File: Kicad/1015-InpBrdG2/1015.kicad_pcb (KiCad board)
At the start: 2 copper layers, 44.5 x 20.3 mm, 10 parts, among them P1 TST, P2 CONN_4, P3 CONN_4, P4 CONN_6, P5 CONN_8, P6 CONN_4

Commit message: Updates to silkscreen and created mashup.  These Gerbers sent to PCB house.
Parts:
- R1: value 100K -> 0
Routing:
- added copper zone on B.Cu, net GND
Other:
- board text added: "CLK"
- board text added: "MISO"
- board text added: "MOSI"
- board text added: "SSEL"
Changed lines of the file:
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@@
     (links 18)
     (no_connects 0)
-    (area 221.843599 152.39619 267.97127 176.403)
+    (area 220.904999 154.533599 265.836401 175.831501)
     (thickness 1.6)
-    (drawings 4)
+    (drawings 8)
     (tracks 21)
     (zones 0)
@@
   )
   (setup
-    (last_trace_width 0.889)
-    (user_trace_width 0.889)
+    (last_trace_width 0.254)
+    (user_trace_width 1.27)
     (trace_clearance 0.254)
-    (zone_clearance 0.254)
+    (zone_clearance 0.508)
     (zone_45_only no)
     (trace_min 0.254)
@@
     (autoplace_cost90 10)
     (autoplace_cost180 10)
-    (fp_text reference R2 (at -1.016 2.54 180) (layer F.SilkS)
-      (effects (font (size 1.397 1.27) (thickness 0.2032)))
-    )
-    (fp_text value 480 (at -1.143 2.54 180) (layer F.SilkS) hide
+    (fp_text reference R2 (at 3.81 0 180) (layer F.SilkS)
+      (effects (font (size 1.397 1.27) (thickness 0.2032)))
+    )
+    (fp_text value 480 (at -0.635 -0.635 180) (layer F.SilkS) hide
       (effects (font (size 1.397 1.27) (thickness 0.2032)))
     )
@@
     (autoplace_cost90 10)
     (autoplace_cost180 10)
-    (fp_text reference R3 (at -1.016 2.54 180) (layer F.SilkS)
-      (effects (font (size 1.397 1.27) (thickness 0.2032)))
-    )
-    (fp_text value 480 (at -1.143 2.54 180) (layer F.SilkS) hide
+    (fp_text reference R3 (at 3.81 0 180) (layer F.SilkS)
+      (effects (font (size 1.397 1.27) (thickness 0.2032)))
+    )
+    (fp_text value 480 (at 0 0 180) (layer F.SilkS) hide
       (effects (font (size 1.397 1.27) (thickness 0.2032)))
     )
@@
     (autoplace_cost90 10)
     (autoplace_cost180 10)
-    (fp_text reference R4 (at -1.016 2.54 180) (layer F.SilkS)
-      (effects (font (size 1.397 1.27) (thickness 0.2032)))
-    )
-    (fp_text value 480 (at -1.143 2.54 180) (layer F.SilkS) hide
+    (fp_text reference R4 (at 3.81 -0.635 180) (layer F.SilkS)
+      (effects (font (size 1.397 1.27) (thickness 0.2032)))
+    )
+    (fp_text value 480 (at 0 0 180) (layer F.SilkS) hide
       (effects (font (size 1.397 1.27) (thickness 0.2032)))
     )
@@
   (module 00_th1x6x100-lock (layer F.Cu)
     (at 239.395 162.56 270)
-    (fp_text reference P4 (at -6.35 5.08 360) (layer F.SilkS)
+    (fp_text reference P4 (at 5.08 -5.08 270) (layer F.SilkS)
       (effects (font (size 1.524 1.524) (thickness 0.3048)))
     )
@@
       (effects (font (size 1.397 1.27) (thickness 0.2032)))
     )
-    (fp_text value 100K (at 0 0.127 180) (layer F.SilkS)
+    (fp_text value 0 (at 0 0.127 180) (layer F.SilkS)
       (effects (font (size 1.397 1.27) (thickness 0.2032)))
     )
@@
     )
   )
+  (gr_text SSEL (at 245.745 163.195) (layer F.SilkS)
+    (effects (font (size 1.5 1.5) (thickness 0.3)))
+  )
+  (gr_text CLK (at 245.11 161.29) (layer F.SilkS)
+    (effects (font (size 1.5 1.5) (thickness 0.3)))
+  )
+  (gr_text MISO (at 245.745 158.75) (layer F.SilkS)
+    (effects (font (size 1.5 1.5) (thickness 0.3)))
+  )
+  (gr_text MOSI (at 245.745 156.21) (layer F.SilkS)
+    (effects (font (size 1.5 1.5) (thickness 0.3)))
+  )
   (gr_line (start 265.43 154.94) (end 220.98 154.94) (angle 90) (layer Edge.Cuts) (width 0.15))
   (gr_line (start 265.43 175.26) (end 265.43 154.94) (angle 90) (layer Edge.Cuts) (width 0.15))
   (gr_line (start 220.98 175.26) (end 265.43 175.26) (angle 90) (layer Edge.Cuts) (width 0.15))
   (gr_line (start 220.98 154.94) (end 220.98 175.26) (angle 90) (layer Edge.Cuts) (width 0.15))
-  (segment (start 226.06 156.21) (end 226.06 173.99) (width 0.889) (layer F.Cu) (net 1) (status C00000))
-  (segment (start 228.6 156.21) (end 228.6 173.99) (width 0.889) (layer F.Cu) (net 2) (status C00000))
+  (segment (start 226.06 156.21) (end 226.06 173.99) (width 1.27) (layer F.Cu) (net 1))
+  (segment (start 228.6 156.21) (end 228.6 173.99) (width 1.27) (layer F.Cu) (net 2))
   (segment (start 264.16 156.21) (end 260.985 156.21) (width 0.254) (layer F.Cu) (net 3))
   (segment (start 260.985 156.21) (end 260.35 156.845) (width 0.254) (layer F.Cu) (net 3))
@@
   (segment (start 257.81 163.195) (end 240.03 163.195) (width 0.254) (layer F.Cu) (net 13))
   (segment (start 240.03 163.195) (end 239.395 163.83) (width 0.254) (layer F.Cu) (net 13))
-  (segment (start 239.395 168.91) (end 231.14 168.91) (width 0.889) (layer F.Cu) (net 14) (status 400000))
-  (segment (start 231.14 160.02) (end 231.14 168.91) (width 0.889) (layer F.Cu) (net 14) (status 400000))
-  (segment (start 231.14 168.91) (end 231.14 173.99) (width 0.889) (layer F.Cu) (net 14) (status 800000))
-  (segment (start 231.14 156.21) (end 231.14 160.02) (width 0.889) (layer F.Cu) (net 14) (status C00000))
+  (segment (start 239.395 168.91) (end 231.14 168.91) (width 1.27) (layer F.Cu) (net 14))
+  (segment (start 231.14 160.02) (end 231.14 168.91) (width 1.27) (layer F.Cu) (net 14))
+  (segment (start 231.14 168.91) (end 231.14 173.99) (width 1.27) (layer F.Cu) (net 14))
+  (segment (start 231.14 156.21) (end 231.14 160.02) (width 0.889) (layer F.Cu) (net 14))
   (zone (net 15) (net_name GNDPWR) (layer B.Cu) (hatch edge 0.508)
     (connect_pads (clearance 0.254))
@@
     (polygon
       (pts
-        (xy 232.41 154.94) (xy 232.41 175.26) (xy 220.98 175.26) (xy 220.98 154.94)
+        (xy 228.6 154.94) (xy 228.6 175.26) (xy 220.98 175.26) (xy 220.98 154.94)
       )
     )
+  )
+  (zone (net 14) (net_name GND) (layer B.Cu) (hatch edge 0.508)
+    (connect_pads (clearance 0.508))
+    (min_thickness 0.254)
+    (fill (arc_segments 16) (thermal_gap 0.508) (thermal_bridge_width 0.508))
+    (polygon
+      (pts
+        (xy 265.43 175.26) (xy 229.87 175.26) (xy 229.87 154.94) (xy 265.43 154.94)
+      )
+    )

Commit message: Added OPP logo to all boards.  Better late than never.
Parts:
- added VAL: REF, opp_logo_backsilk, F.Cu at (248.9, 171.4)

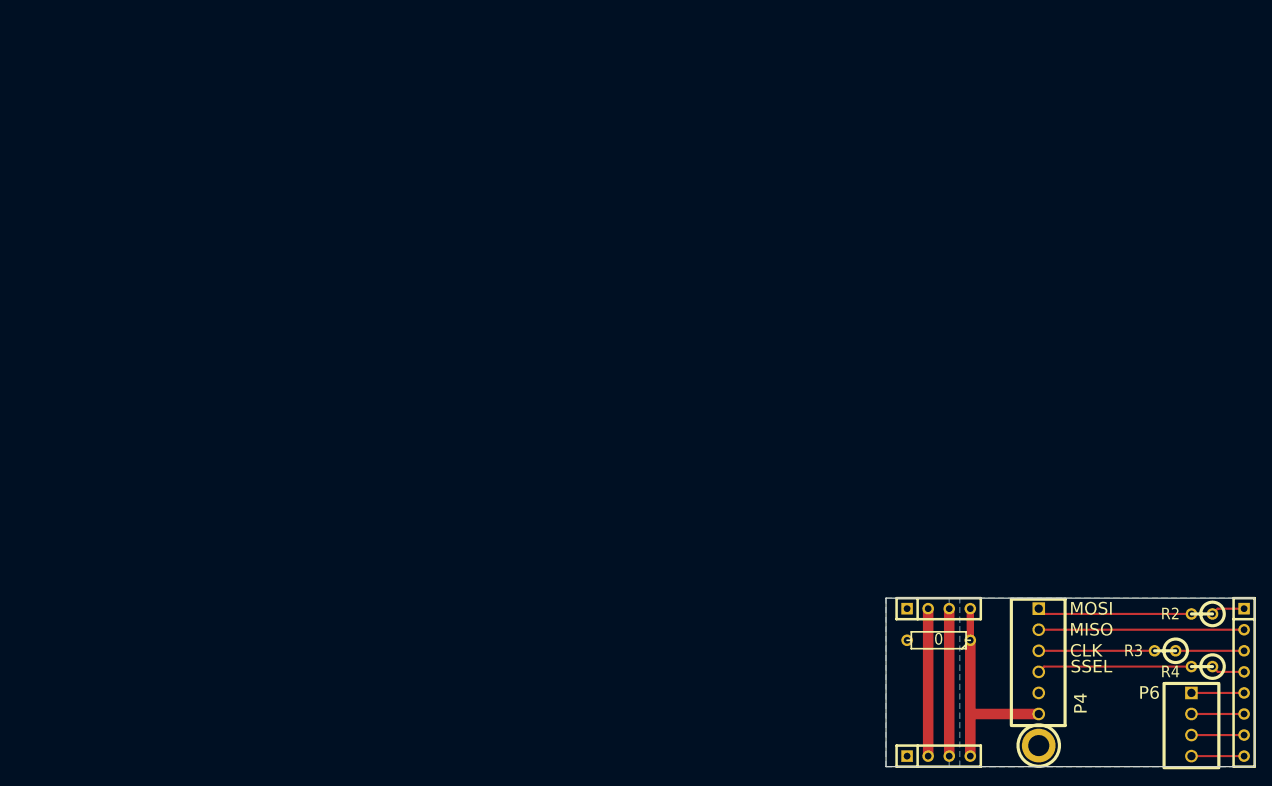
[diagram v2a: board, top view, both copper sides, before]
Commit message: Changed size of PCB sheets to 8.5" x 11".  Added name/rev/board name to PCB sheets.
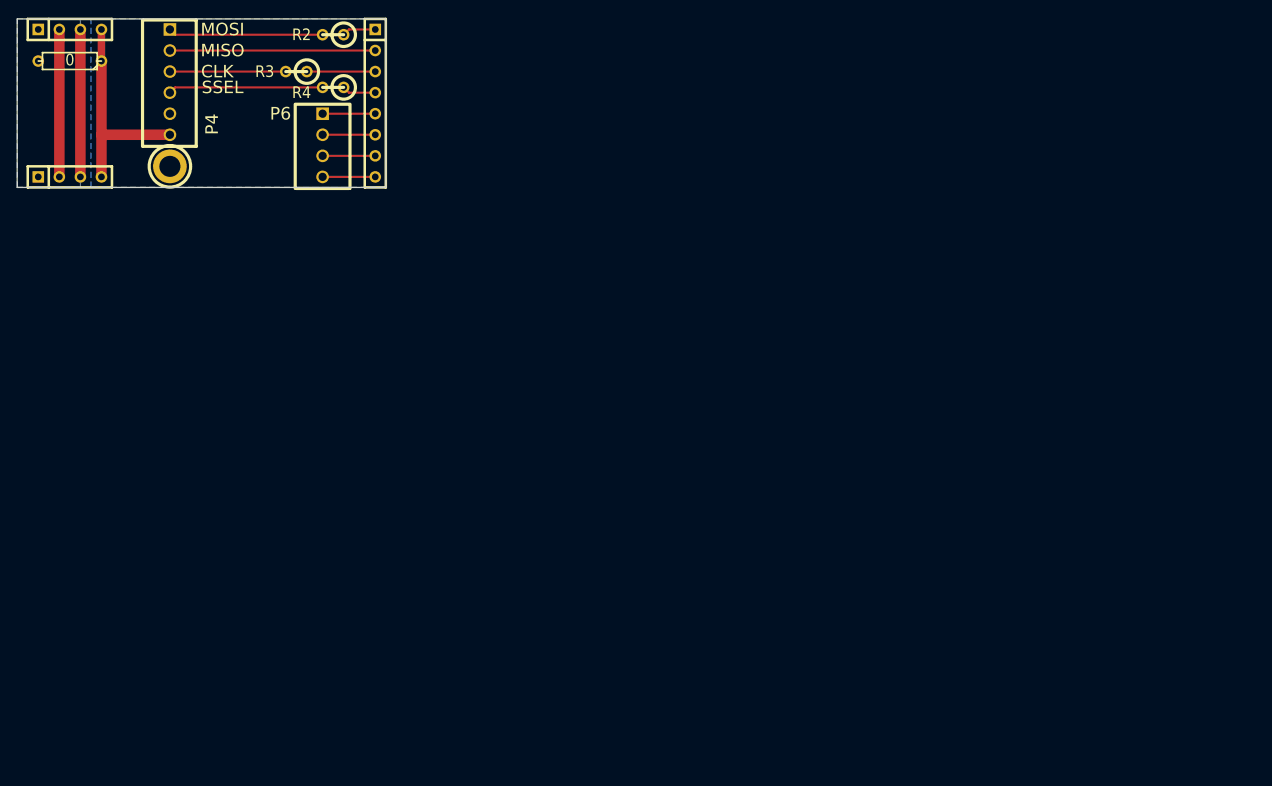
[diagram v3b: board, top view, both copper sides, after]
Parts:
- moved P1 125.9 mm to (134.6, 102.9)
- moved P2 125.9 mm to (122.6, 104.1)
- moved P3 125.9 mm to (122.6, 86.4)
- moved P4 125.9 mm to (134.6, 92.7)
- moved P5 125.9 mm to (159.4, 95.2)
- moved P6 125.9 mm to (153.0, 100.3)
- moved R1 125.9 mm to (122.6, 90.2)
- moved R2 125.9 mm to (154.3, 87.0)
- moved R3 125.9 mm to (149.9, 91.4)
- moved R4 125.9 mm to (154.3, 93.3)
- moved VAL 125.9 mm to (144.1, 101.6)
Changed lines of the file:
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@@
     (nets 16)
   )
-  (page A3)
+  (page A)
+  (title_block
+    (title "Input Board (Gen 2)")
+    (rev -)
+    (company "Open Pinball Project")
+  )
   (layers
     (15 F.Cu signal)
@@
   )
   (module SIL-8 (layer F.Cu)
-    (at 264.16 165.1 270)
+    (at 159.385 95.25 270)
     (descr "Connecteur 8 pins")
     (tags "CONN DEV")
@@
   )
   (module SIL-4 (layer F.Cu)
-    (at 227.33 173.99)
+    (at 122.555 104.14)
     (descr "Connecteur 4 pibs")
     (tags "CONN DEV")
@@
   )
   (module SIL-4 (layer F.Cu)
-    (at 227.33 156.21)
+    (at 122.555 86.36)
     (descr "Connecteur 4 pibs")
     (tags "CONN DEV")
@@
   )
   (module R1 (layer F.Cu)
-    (at 259.08 156.845 180)
+    (at 154.305 86.995 180)
     (descr "Resistance verticale")
     (tags R)
@@
   )
   (module R1 (layer F.Cu)
-    (at 254.635 161.29 180)
+    (at 149.86 91.44 180)
     (descr "Resistance verticale")
     (tags R)
@@
   )
   (module R1 (layer F.Cu)
-    (at 259.08 163.195 180)
+    (at 154.305 93.345 180)
     (descr "Resistance verticale")
     (tags R)
@@
   )
   (module 00_th1x6x100-lock (layer F.Cu)
-    (at 239.395 162.56 270)
+    (at 134.62 92.71 270)
     (fp_text reference P4 (at 5.08 -5.08 270) (layer F.SilkS)
       (effects (font (size 1.524 1.524) (thickness 0.3048)))
@@
   )
   (module 00_th1x4x100-lock (layer F.Cu)
-    (at 257.81 170.18 270)
+    (at 153.035 100.33 270)
     (fp_text reference P6 (at -3.81 5.08 360) (layer F.SilkS)
       (effects (font (size 1.524 1.524) (thickness 0.3048)))
@@
   )
   (module 00_mtg_hole-2-56 (layer F.Cu)
-    (at 239.395 172.72)
+    (at 134.62 102.87)
     (descr "module 1 pin (ou trou mecanique de percage)")
     (tags DEV)
@@
   )
   (module R3 (layer F.Cu)
-    (at 227.33 160.02 180)
+    (at 122.555 90.17 180)
     (descr "Resitance 3 pas")
     (tags R)
@@
   )
   (module opp_logo_backsilk (layer F.Cu)
-    (at 248.92 171.45)
+    (at 144.145 101.6)
     (fp_text reference VAL (at 0 0) (layer F.SilkS) hide
       (effects (font (size 0.381 0.381) (thickness 0.127)))
@@
       (xy -1.6764 -1.524) (xy -1.7145 -1.50114) (xy -1.7272 -1.47066) (xy -1.7272 -1.47066)) (layer B.SilkS) (width 0.00254))
   )
-  (gr_text SSEL (at 245.745 163.195) (layer F.SilkS)
+  (gr_text SSEL (at 140.97 93.345) (layer F.SilkS)
     (effects (font (size 1.5 1.5) (thickness 0.3)))
   )
-  (gr_text CLK (at 245.11 161.29) (layer F.SilkS)
+  (gr_text CLK (at 140.335 91.44) (layer F.SilkS)
     (effects (font (size 1.5 1.5) (thickness 0.3)))
   )
-  (gr_text MISO (at 245.745 158.75) (layer F.SilkS)
+  (gr_text MISO (at 140.97 88.9) (layer F.SilkS)
     (effects (font (size 1.5 1.5) (thickness 0.3)))
   )
-  (gr_text MOSI (at 245.745 156.21) (layer F.SilkS)
+  (gr_text MOSI (at 140.97 86.36) (layer F.SilkS)
     (effects (font (size 1.5 1.5) (thickness 0.3)))
   )
-  (gr_line (start 265.43 154.94) (end 220.98 154.94) (angle 90) (layer Edge.Cuts) (width 0.15))
-  (gr_line (start 265.43 175.26) (end 265.43 154.94) (angle 90) (layer Edge.Cuts) (width 0.15))
-  (gr_line (start 220.98 175.26) (end 265.43 175.26) (angle 90) (layer Edge.Cuts) (width 0.15))
-  (gr_line (start 220.98 154.94) (end 220.98 175.26) (angle 90) (layer Edge.Cuts) (width 0.15))
-  (segment (start 226.06 156.21) (end 226.06 173.99) (width 1.27) (layer F.Cu) (net 1))
-  (segment (start 228.6 156.21) (end 228.6 173.99) (width 1.27) (layer F.Cu) (net 2))
-  (segment (start 264.16 156.21) (end 260.985 156.21) (width 0.254) (layer F.Cu) (net 3))
-  (segment (start 260.985 156.21) (end 260.35 156.845) (width 0.254) (layer F.Cu) (net 3))
-  (segment (start 264.16 158.75) (end 239.395 158.75) (width 0.254) (layer F.Cu) (net 4))
-  (segment (start 264.16 161.29) (end 255.905 161.29) (width 0.254) (layer F.Cu) (net 5))
-  (segment (start 264.16 163.83) (end 260.985 163.83) (width 0.254) (layer F.Cu) (net 6))
-  (segment (start 260.985 163.83) (end 260.35 163.195) (width 0.254) (layer F.Cu) (net 6))
-  (segment (start 264.16 166.37) (end 257.81 166.37) (width 0.254) (layer F.Cu) (net 7))
-  (segment (start 264.16 168.91) (end 257.81 168.91) (width 0.254) (layer F.Cu) (net 8))
-  (segment (start 264.16 171.45) (end 257.81 171.45) (width 0.254) (layer F.Cu) (net 9))
-  (segment (start 264.16 173.99) (end 257.81 173.99) (width 0.254) (layer F.Cu) (net 10))
-  (segment (start 253.365 161.29) (end 239.395 161.29) (width 0.254) (layer F.Cu) (net 11))
-  (segment (start 257.81 156.845) (end 240.03 156.845) (width 0.254) (layer F.Cu) (net 12))
-  (segment (start 240.03 156.845) (end 239.395 156.21) (width 0.254) (layer F.Cu) (net 12))
-  (segment (start 257.81 163.195) (end 240.03 163.195) (width 0.254) (layer F.Cu) (net 13))
-  (segment (start 240.03 163.195) (end 239.395 163.83) (width 0.254) (layer F.Cu) (net 13))
-  (segment (start 239.395 168.91) (end 231.14 168.91) (width 1.27) (layer F.Cu) (net 14))
-  (segment (start 231.14 160.02) (end 231.14 168.91) (width 1.27) (layer F.Cu) (net 14))
-  (segment (start 231.14 168.91) (end 231.14 173.99) (width 1.27) (layer F.Cu) (net 14))
-  (segment (start 231.14 156.21) (end 231.14 160.02) (width 0.889) (layer F.Cu) (net 14))
+  (gr_line (start 160.655 85.09) (end 116.205 85.09) (angle 90) (layer Edge.Cuts) (width 0.15))
+  (gr_line (start 160.655 105.41) (end 160.655 85.09) (angle 90) (layer Edge.Cuts) (width 0.15))
+  (gr_line (start 116.205 105.41) (end 160.655 105.41) (angle 90) (layer Edge.Cuts) (width 0.15))
+  (gr_line (start 116.205 85.09) (end 116.205 105.41) (angle 90) (layer Edge.Cuts) (width 0.15))
+  (segment (start 121.285 86.36) (end 121.285 104.14) (width 1.27) (layer F.Cu) (net 1))
+  (segment (start 123.825 86.36) (end 123.825 104.14) (width 1.27) (layer F.Cu) (net 2))
+  (segment (start 159.385 86.36) (end 156.21 86.36) (width 0.254) (layer F.Cu) (net 3))
+  (segment (start 156.21 86.36) (end 155.575 86.995) (width 0.254) (layer F.Cu) (net 3))
+  (segment (start 159.385 88.9) (end 134.62 88.9) (width 0.254) (layer F.Cu) (net 4))
+  (segment (start 159.385 91.44) (end 151.13 91.44) (width 0.254) (layer F.Cu) (net 5))
+  (segment (start 159.385 93.98) (end 156.21 93.98) (width 0.254) (layer F.Cu) (net 6))
+  (segment (start 156.21 93.98) (end 155.575 93.345) (width 0.254) (layer F.Cu) (net 6))
+  (segment (start 159.385 96.52) (end 153.035 96.52) (width 0.254) (layer F.Cu) (net 7))
+  (segment (start 159.385 99.06) (end 153.035 99.06) (width 0.254) (layer F.Cu) (net 8))
+  (segment (start 159.385 101.6) (end 153.035 101.6) (width 0.254) (layer F.Cu) (net 9))
+  (segment (start 159.385 104.14) (end 153.035 104.14) (width 0.254) (layer F.Cu) (net 10))
+  (segment (start 148.59 91.44) (end 134.62 91.44) (width 0.254) (layer F.Cu) (net 11))
+  (segment (start 153.035 86.995) (end 135.255 86.995) (width 0.254) (layer F.Cu) (net 12))
+  (segment (start 135.255 86.995) (end 134.62 86.36) (width 0.254) (layer F.Cu) (net 12))
+  (segment (start 153.035 93.345) (end 135.255 93.345) (width 0.254) (layer F.Cu) (net 13))
+  (segment (start 135.255 93.345) (end 134.62 93.98) (width 0.254) (layer F.Cu) (net 13))
+  (segment (start 134.62 99.06) (end 126.365 99.06) (width 1.27) (layer F.Cu) (net 14))
+  (segment (start 126.365 90.17) (end 126.365 99.06) (width 1.27) (layer F.Cu) (net 14))
+  (segment (start 126.365 99.06) (end 126.365 104.14) (width 1.27) (layer F.Cu) (net 14))
+  (segment (start 126.365 86.36) (end 126.365 90.17) (width 0.889) (layer F.Cu) (net 14))
   (zone (net 15) (net_name GNDPWR) (layer B.Cu) (hatch edge 0.508)
     (connect_pads (clearance 0.254))
@@
     (polygon
       (pts
-        (xy 228.6 154.94) (xy 228.6 175.26) (xy 220.98 175.26) (xy 220.98 154.94)
+        (xy 123.825 85.09) (xy 123.825 105.41) (xy 116.205 105.41) (xy 116.205 85.09)
       )
     )
@@
     (polygon
       (pts
-        (xy 265.43 175.26) (xy 229.87 175.26) (xy 229.87 154.94) (xy 265.43 154.94)
+        (xy 160.655 105.41) (xy 125.095 105.41) (xy 125.095 85.09) (xy 160.655 85.09)
       )
     )
